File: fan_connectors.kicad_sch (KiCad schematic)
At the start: 4 parts, among them J1701 Molex 470531000, J1702 HC-1.0-4PLT

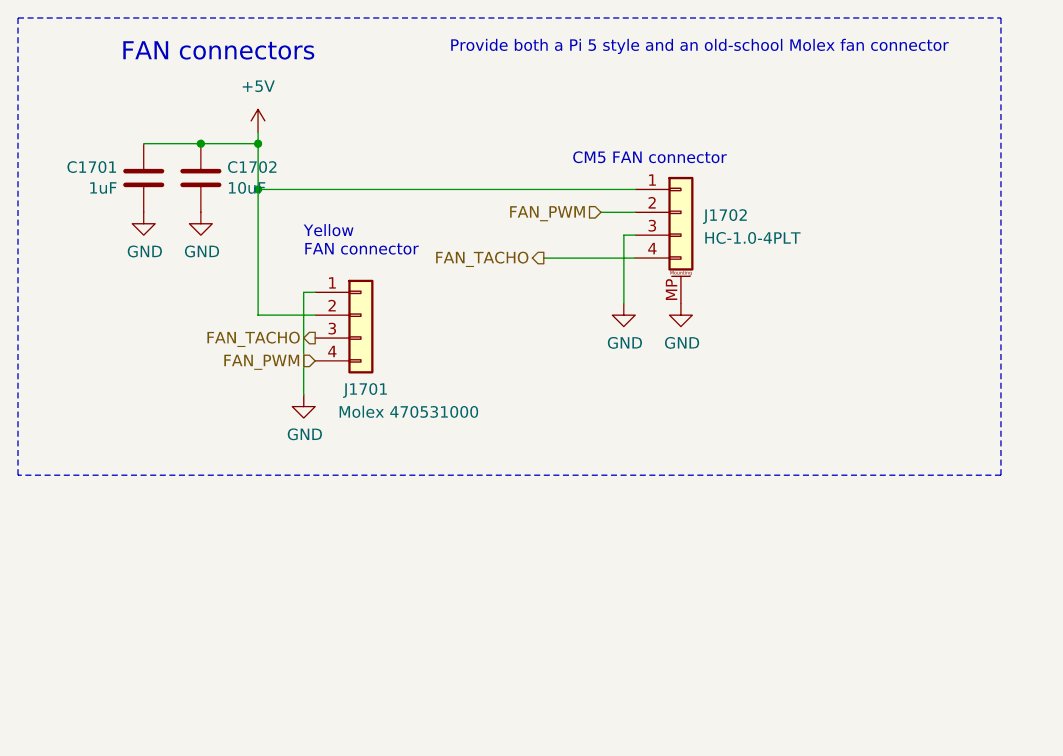
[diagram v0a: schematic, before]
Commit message: Remove Molex fan connector, add another CM5 connector to board bottom
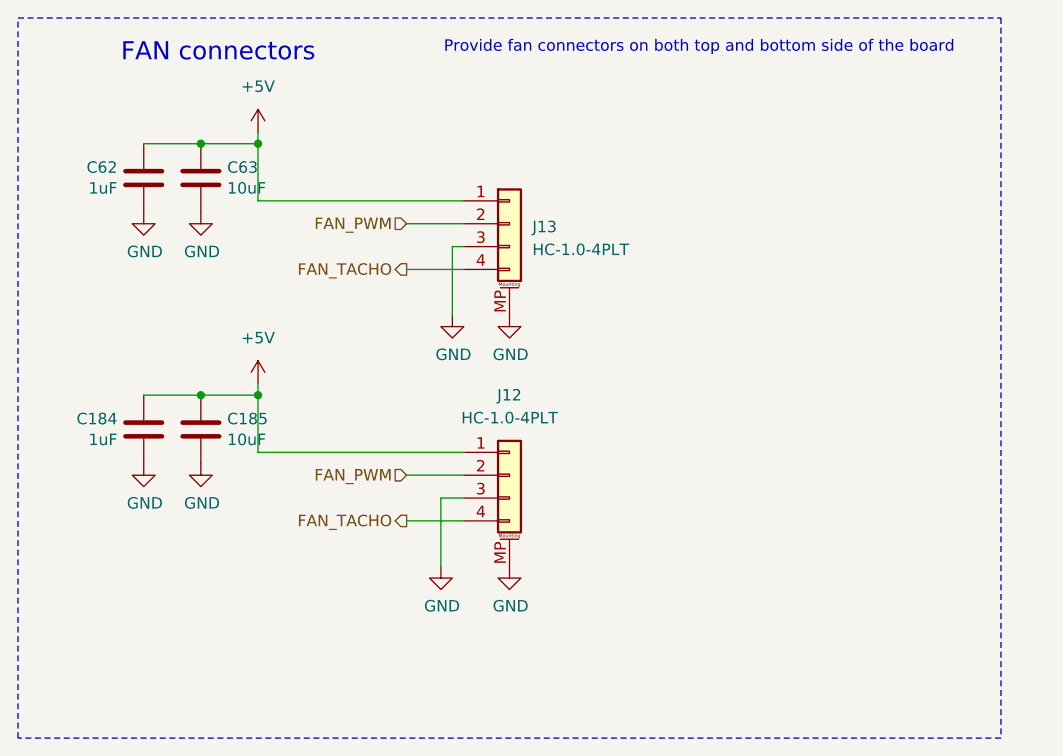
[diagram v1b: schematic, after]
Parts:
- removed J1701: Molex 470531000, Connector:FanPinHeader_1x04_P2.54mm_Vertical, symbol Connector_Generic:Conn_01x04
- added C184: 1uF, Capacitor_SMD:C_0402_1005Metric, symbol Device:C
- added C185: 10uF, Capacitor_SMD:C_0603_1608Metric, symbol Device:C
- added J12: HC-1.0-4PLT, Hatlabs:JST_SH_HCTL_HC-1.0-4PLT_1x04-1MP_P1.00mm_Vertical, symbol Connector_Generic_MountingPin:Conn_01x04_MountingPin
- renumbered C1701 to C62, C1702 to C63, J1702 to J13
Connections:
- net +5V: now also C184.1, C185.1, J12.1 (Pin_1)
- net FAN_PWM: now also J12.2 (Pin_2)
- net FAN_TACHO: now also J12.4 (Pin_4)
- net GND: now also C184.2, C185.2, J12.3 (Pin_3), J12.MP (MountPin)
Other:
- note added: "Provide fan connectors on both top and bottom side of the board"
- note removed: "CM5 FAN connector"
- note removed: "Provide both a Pi 5 style and an old-school Molex fan connector"
- note removed: "Yellow FAN connector"
- moved on the sheet: J13

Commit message: Reannotate the board
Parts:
- renumbered C62 to C61, C184 to C62, C185 to C64, J13 to J12, J12 to J13
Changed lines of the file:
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@@
 		(on_board yes)
 		(dnp no)
-		(property "Reference" "#PWR0106"
+		(property "Reference" "#PWR0104"
 			(at 133.35 107.95 0)
 			(effects
@@
 			(project "HALPI2"
 				(path "/abc482bd-3f17-4d35-80db-1da3dcdb5c27/7c248bd3-8232-4777-a40c-eab53460cf85/1b14d1cb-dda2-44c5-97d1-a618f21bed66"
-					(reference "#PWR0106")
+					(reference "#PWR0104")
 					(unit 1)
 				)
@@
 		(on_board yes)
 		(dnp no)
-		(property "Reference" "C62"
+		(property "Reference" "C61"
 			(at 96.139 85.1916 0)
 			(effects
@@
 			(project "HALPI2"
 				(path "/abc482bd-3f17-4d35-80db-1da3dcdb5c27/7c248bd3-8232-4777-a40c-eab53460cf85/1b14d1cb-dda2-44c5-97d1-a618f21bed66"
-					(reference "C62")
+					(reference "C61")
 					(unit 1)
 				)
@@
 		(on_board yes)
 		(dnp no)
-		(property "Reference" "#PWR0102"
+		(property "Reference" "#PWR099"
 			(at 105.41 96.52 0)
 			(effects
@@
 			(project "HALPI2"
 				(path "/abc482bd-3f17-4d35-80db-1da3dcdb5c27/7c248bd3-8232-4777-a40c-eab53460cf85/1b14d1cb-dda2-44c5-97d1-a618f21bed66"
-					(reference "#PWR0102")
+					(reference "#PWR099")
 					(unit 1)
 				)
@@
 		(on_board yes)
 		(dnp no)
-		(property "Reference" "#PWR0101"
+		(property "Reference" "#PWR097"
 			(at 99.06 96.52 0)
 			(effects
@@
 			(project "HALPI2"
 				(path "/abc482bd-3f17-4d35-80db-1da3dcdb5c27/7c248bd3-8232-4777-a40c-eab53460cf85/1b14d1cb-dda2-44c5-97d1-a618f21bed66"
-					(reference "#PWR0101")
+					(reference "#PWR097")
 					(unit 1)
 				)
@@
 		(on_board yes)
 		(dnp no)
-		(property "Reference" "#PWR0355"
+		(property "Reference" "#PWR0100"
 			(at 105.41 124.46 0)
 			(effects
@@
 			(project "HALPI2"
 				(path "/abc482bd-3f17-4d35-80db-1da3dcdb5c27/7c248bd3-8232-4777-a40c-eab53460cf85/1b14d1cb-dda2-44c5-97d1-a618f21bed66"
-					(reference "#PWR0355")
+					(reference "#PWR0100")
 					(unit 1)
 				)
@@
 		(on_board yes)
 		(dnp no)
-		(property "Reference" "C185"
+		(property "Reference" "C64"
 			(at 108.331 113.1316 0)
 			(effects
@@
 			(project "HALPI2"
 				(path "/abc482bd-3f17-4d35-80db-1da3dcdb5c27/7c248bd3-8232-4777-a40c-eab53460cf85/1b14d1cb-dda2-44c5-97d1-a618f21bed66"
-					(reference "C185")
+					(reference "C64")
 					(unit 1)
 				)
@@
 		(on_board yes)
 		(dnp no)
-		(property "Reference" "#PWR0104"
+		(property "Reference" "#PWR0103"
 			(at 132.08 135.89 0)
 			(effects
@@
 			(project "HALPI2"
 				(path "/abc482bd-3f17-4d35-80db-1da3dcdb5c27/7c248bd3-8232-4777-a40c-eab53460cf85/1b14d1cb-dda2-44c5-97d1-a618f21bed66"
-					(reference "#PWR0104")
+					(reference "#PWR0103")
 					(unit 1)
 				)
@@
 		(on_board yes)
 		(dnp no)
-		(property "Reference" "#PWR0354"
+		(property "Reference" "#PWR098"
 			(at 99.06 124.46 0)
 			(effects
@@
 			(project "HALPI2"
 				(path "/abc482bd-3f17-4d35-80db-1da3dcdb5c27/7c248bd3-8232-4777-a40c-eab53460cf85/1b14d1cb-dda2-44c5-97d1-a618f21bed66"
-					(reference "#PWR0354")
+					(reference "#PWR098")
 					(unit 1)
 				)
@@
 		(dnp no)
 		(fields_autoplaced yes)
-		(property "Reference" "#PWR0103"
+		(property "Reference" "#PWR0101"
 			(at 111.76 85.09 0)
 			(effects
@@
 			(project "HALPI2"
 				(path "/abc482bd-3f17-4d35-80db-1da3dcdb5c27/7c248bd3-8232-4777-a40c-eab53460cf85/1b14d1cb-dda2-44c5-97d1-a618f21bed66"
-					(reference "#PWR0103")
+					(reference "#PWR0101")
 					(unit 1)
 				)
@@
 		(dnp no)
 		(fields_autoplaced yes)
-		(property "Reference" "#PWR0356"
+		(property "Reference" "#PWR0102"
 			(at 111.76 113.03 0)
 			(effects
@@
 			(project "HALPI2"
 				(path "/abc482bd-3f17-4d35-80db-1da3dcdb5c27/7c248bd3-8232-4777-a40c-eab53460cf85/1b14d1cb-dda2-44c5-97d1-a618f21bed66"
-					(reference "#PWR0356")
+					(reference "#PWR0102")
 					(unit 1)
 				)
@@
 		(on_board yes)
 		(dnp no)
-		(property "Reference" "#PWR0107"
+		(property "Reference" "#PWR0105"
 			(at 139.7 107.95 0)
 			(effects
@@
 			(project "HALPI2"
 				(path "/abc482bd-3f17-4d35-80db-1da3dcdb5c27/7c248bd3-8232-4777-a40c-eab53460cf85/1b14d1cb-dda2-44c5-97d1-a618f21bed66"
-					(reference "#PWR0107")
+					(reference "#PWR0105")
 					(unit 1)
 				)
@@
 		(on_board yes)
 		(dnp no)
-		(property "Reference" "C184"
+		(property "Reference" "C62"
 			(at 96.139 113.1316 0)
 			(effects
@@
 			(project "HALPI2"
 				(path "/abc482bd-3f17-4d35-80db-1da3dcdb5c27/7c248bd3-8232-4777-a40c-eab53460cf85/1b14d1cb-dda2-44c5-97d1-a618f21bed66"
-					(reference "C184")
+					(reference "C62")
 					(unit 1)
 				)
@@
 		(dnp no)
 		(fields_autoplaced yes)
-		(property "Reference" "J13"
+		(property "Reference" "J12"
 			(at 142.24 91.7955 0)
 			(effects
@@
 			(project "HALPI2"
 				(path "/abc482bd-3f17-4d35-80db-1da3dcdb5c27/7c248bd3-8232-4777-a40c-eab53460cf85/1b14d1cb-dda2-44c5-97d1-a618f21bed66"
-					(reference "J13")
+					(reference "J12")
 					(unit 1)
 				)
@@
 		(dnp no)
 		(fields_autoplaced yes)
-		(property "Reference" "J12"
+		(property "Reference" "J13"
 			(at 139.7 110.49 0)
 			(effects
@@
 			(project "HALPI2"
 				(path "/abc482bd-3f17-4d35-80db-1da3dcdb5c27/7c248bd3-8232-4777-a40c-eab53460cf85/1b14d1cb-dda2-44c5-97d1-a618f21bed66"
-					(reference "J12")
+					(reference "J13")
 					(unit 1)
 				)
@@
 		(on_board yes)
 		(dnp no)
-		(property "Reference" "#PWR0105"
+		(property "Reference" "#PWR0106"
 			(at 139.7 135.89 0)
 			(effects
@@
 			(project "HALPI2"
 				(path "/abc482bd-3f17-4d35-80db-1da3dcdb5c27/7c248bd3-8232-4777-a40c-eab53460cf85/1b14d1cb-dda2-44c5-97d1-a618f21bed66"
-					(reference "#PWR0105")
-					(unit 1)
-				)
+					(reference "#PWR0106")
+					(unit 1)
+				)

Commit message: FInal v0.2.0 proto changes
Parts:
- renumbered C61 to C63, C62 to C64, C63 to C65, C64 to C66
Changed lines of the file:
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@@
 		(on_board yes)
 		(dnp no)
-		(property "Reference" "C63"
+		(property "Reference" "C65"
 			(at 108.331 85.1916 0)
 			(effects
@@
 			(project "HALPI2"
 				(path "/abc482bd-3f17-4d35-80db-1da3dcdb5c27/7c248bd3-8232-4777-a40c-eab53460cf85/1b14d1cb-dda2-44c5-97d1-a618f21bed66"
-					(reference "C63")
+					(reference "C65")
 					(unit 1)
 				)
@@
 		(on_board yes)
 		(dnp no)
-		(property "Reference" "#PWR0104"
+		(property "Reference" "#PWR0105"
 			(at 133.35 107.95 0)
 			(effects
@@
 			(project "HALPI2"
 				(path "/abc482bd-3f17-4d35-80db-1da3dcdb5c27/7c248bd3-8232-4777-a40c-eab53460cf85/1b14d1cb-dda2-44c5-97d1-a618f21bed66"
-					(reference "#PWR0104")
+					(reference "#PWR0105")
 					(unit 1)
 				)
@@
 		(on_board yes)
 		(dnp no)
-		(property "Reference" "C61"
+		(property "Reference" "C63"
 			(at 96.139 85.1916 0)
 			(effects
@@
 			(project "HALPI2"
 				(path "/abc482bd-3f17-4d35-80db-1da3dcdb5c27/7c248bd3-8232-4777-a40c-eab53460cf85/1b14d1cb-dda2-44c5-97d1-a618f21bed66"
-					(reference "C61")
+					(reference "C63")
 					(unit 1)
 				)
@@
 		(on_board yes)
 		(dnp no)
-		(property "Reference" "#PWR099"
+		(property "Reference" "#PWR0100"
 			(at 105.41 96.52 0)
 			(effects
@@
 			(project "HALPI2"
 				(path "/abc482bd-3f17-4d35-80db-1da3dcdb5c27/7c248bd3-8232-4777-a40c-eab53460cf85/1b14d1cb-dda2-44c5-97d1-a618f21bed66"
-					(reference "#PWR099")
+					(reference "#PWR0100")
 					(unit 1)
 				)
@@
 		(on_board yes)
 		(dnp no)
-		(property "Reference" "#PWR097"
+		(property "Reference" "#PWR098"
 			(at 99.06 96.52 0)
 			(effects
@@
 			(project "HALPI2"
 				(path "/abc482bd-3f17-4d35-80db-1da3dcdb5c27/7c248bd3-8232-4777-a40c-eab53460cf85/1b14d1cb-dda2-44c5-97d1-a618f21bed66"
-					(reference "#PWR097")
+					(reference "#PWR098")
 					(unit 1)
 				)
@@
 		(on_board yes)
 		(dnp no)
-		(property "Reference" "#PWR0100"
+		(property "Reference" "#PWR0101"
 			(at 105.41 124.46 0)
 			(effects
@@
 			(project "HALPI2"
 				(path "/abc482bd-3f17-4d35-80db-1da3dcdb5c27/7c248bd3-8232-4777-a40c-eab53460cf85/1b14d1cb-dda2-44c5-97d1-a618f21bed66"
-					(reference "#PWR0100")
+					(reference "#PWR0101")
 					(unit 1)
 				)
@@
 		(on_board yes)
 		(dnp no)
-		(property "Reference" "C64"
+		(property "Reference" "C66"
 			(at 108.331 113.1316 0)
 			(effects
@@
 			(project "HALPI2"
 				(path "/abc482bd-3f17-4d35-80db-1da3dcdb5c27/7c248bd3-8232-4777-a40c-eab53460cf85/1b14d1cb-dda2-44c5-97d1-a618f21bed66"
-					(reference "C64")
+					(reference "C66")
 					(unit 1)
 				)
@@
 		(on_board yes)
 		(dnp no)
-		(property "Reference" "#PWR0103"
+		(property "Reference" "#PWR0104"
 			(at 132.08 135.89 0)
 			(effects
@@
 			(project "HALPI2"
 				(path "/abc482bd-3f17-4d35-80db-1da3dcdb5c27/7c248bd3-8232-4777-a40c-eab53460cf85/1b14d1cb-dda2-44c5-97d1-a618f21bed66"
-					(reference "#PWR0103")
+					(reference "#PWR0104")
 					(unit 1)
 				)
@@
 		(on_board yes)
 		(dnp no)
-		(property "Reference" "#PWR098"
+		(property "Reference" "#PWR099"
 			(at 99.06 124.46 0)
 			(effects
@@
 			(project "HALPI2"
 				(path "/abc482bd-3f17-4d35-80db-1da3dcdb5c27/7c248bd3-8232-4777-a40c-eab53460cf85/1b14d1cb-dda2-44c5-97d1-a618f21bed66"
-					(reference "#PWR098")
+					(reference "#PWR099")
 					(unit 1)
 				)
@@
 		(dnp no)
 		(fields_autoplaced yes)
-		(property "Reference" "#PWR0101"
+		(property "Reference" "#PWR0102"
 			(at 111.76 85.09 0)
 			(effects
@@
 			(project "HALPI2"
 				(path "/abc482bd-3f17-4d35-80db-1da3dcdb5c27/7c248bd3-8232-4777-a40c-eab53460cf85/1b14d1cb-dda2-44c5-97d1-a618f21bed66"
-					(reference "#PWR0101")
+					(reference "#PWR0102")
 					(unit 1)
 				)
@@
 		(dnp no)
 		(fields_autoplaced yes)
-		(property "Reference" "#PWR0102"
+		(property "Reference" "#PWR0103"
 			(at 111.76 113.03 0)
 			(effects
@@
 			(project "HALPI2"
 				(path "/abc482bd-3f17-4d35-80db-1da3dcdb5c27/7c248bd3-8232-4777-a40c-eab53460cf85/1b14d1cb-dda2-44c5-97d1-a618f21bed66"
-					(reference "#PWR0102")
+					(reference "#PWR0103")
 					(unit 1)
 				)
@@
 		(on_board yes)
 		(dnp no)
-		(property "Reference" "#PWR0105"
+		(property "Reference" "#PWR0106"
 			(at 139.7 107.95 0)
 			(effects
@@
 			(project "HALPI2"
 				(path "/abc482bd-3f17-4d35-80db-1da3dcdb5c27/7c248bd3-8232-4777-a40c-eab53460cf85/1b14d1cb-dda2-44c5-97d1-a618f21bed66"
-					(reference "#PWR0105")
+					(reference "#PWR0106")
 					(unit 1)
 				)
@@
 		(on_board yes)
 		(dnp no)
-		(property "Reference" "C62"
+		(property "Reference" "C64"
 			(at 96.139 113.1316 0)
 			(effects
@@
 			(project "HALPI2"
 				(path "/abc482bd-3f17-4d35-80db-1da3dcdb5c27/7c248bd3-8232-4777-a40c-eab53460cf85/1b14d1cb-dda2-44c5-97d1-a618f21bed66"
-					(reference "C62")
+					(reference "C64")
 					(unit 1)
 				)
@@
 		(on_board yes)
 		(dnp no)
-		(property "Reference" "#PWR0106"
+		(property "Reference" "#PWR0107"
 			(at 139.7 135.89 0)
 			(effects
@@
 			(project "HALPI2"
 				(path "/abc482bd-3f17-4d35-80db-1da3dcdb5c27/7c248bd3-8232-4777-a40c-eab53460cf85/1b14d1cb-dda2-44c5-97d1-a618f21bed66"
-					(reference "#PWR0106")
-					(unit 1)
-				)
+					(reference "#PWR0107")
+					(unit 1)
+				)

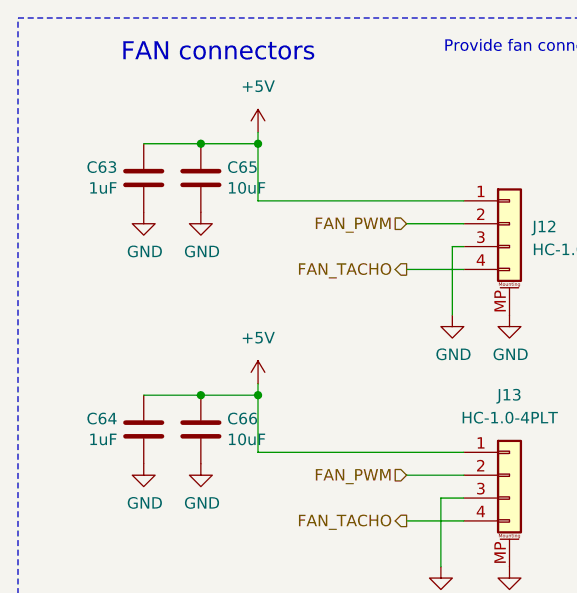
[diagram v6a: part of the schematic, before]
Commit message: Final chores
- Reannotate components
- Improve USB2 connector skew matching
- Update sheet blocks
- Fix some diff-pair double-inversions
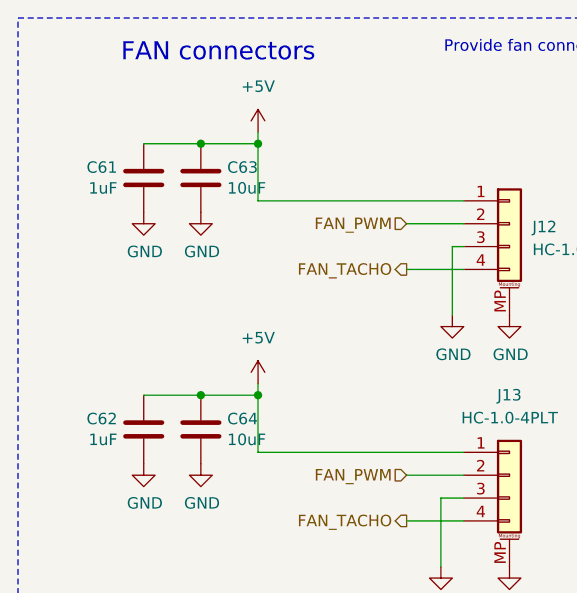
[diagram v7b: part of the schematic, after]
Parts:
- renumbered C63 to C61, C64 to C62, C65 to C63, C66 to C64
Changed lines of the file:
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@@
 	(title_block
 		(title "HALPI2")
-		(date "2025-03-27")
-		(rev "v0.2.0")
+		(date "2025-05-08")
+		(rev "v0.3.0")
 		(company "Hat Labs Oy")
 		(comment 1 "https://ohwr.org/cern_ohl_s_v2.pdf")
@@
 		(on_board yes)
 		(dnp no)
-		(property "Reference" "C65"
+		(property "Reference" "C63"
 			(at 108.331 85.1916 0)
 			(effects
@@
 			(project "HALPI2"
 				(path "/abc482bd-3f17-4d35-80db-1da3dcdb5c27/7c248bd3-8232-4777-a40c-eab53460cf85/1b14d1cb-dda2-44c5-97d1-a618f21bed66"
-					(reference "C65")
+					(reference "C63")
 					(unit 1)
 				)
@@
 		(on_board yes)
 		(dnp no)
-		(property "Reference" "#PWR0105"
+		(property "Reference" "#PWR099"
 			(at 133.35 107.95 0)
 			(effects
@@
 			(project "HALPI2"
 				(path "/abc482bd-3f17-4d35-80db-1da3dcdb5c27/7c248bd3-8232-4777-a40c-eab53460cf85/1b14d1cb-dda2-44c5-97d1-a618f21bed66"
-					(reference "#PWR0105")
+					(reference "#PWR099")
 					(unit 1)
 				)
@@
 		(on_board yes)
 		(dnp no)
-		(property "Reference" "C63"
+		(property "Reference" "C61"
 			(at 96.139 85.1916 0)
 			(effects
@@
 			(project "HALPI2"
 				(path "/abc482bd-3f17-4d35-80db-1da3dcdb5c27/7c248bd3-8232-4777-a40c-eab53460cf85/1b14d1cb-dda2-44c5-97d1-a618f21bed66"
-					(reference "C63")
+					(reference "C61")
 					(unit 1)
 				)
@@
 		(on_board yes)
 		(dnp no)
-		(property "Reference" "#PWR0100"
+		(property "Reference" "#PWR094"
 			(at 105.41 96.52 0)
 			(effects
@@
 			(project "HALPI2"
 				(path "/abc482bd-3f17-4d35-80db-1da3dcdb5c27/7c248bd3-8232-4777-a40c-eab53460cf85/1b14d1cb-dda2-44c5-97d1-a618f21bed66"
-					(reference "#PWR0100")
+					(reference "#PWR094")
 					(unit 1)
 				)
@@
 		(on_board yes)
 		(dnp no)
-		(property "Reference" "#PWR098"
+		(property "Reference" "#PWR092"
 			(at 99.06 96.52 0)
 			(effects
@@
 			(project "HALPI2"
 				(path "/abc482bd-3f17-4d35-80db-1da3dcdb5c27/7c248bd3-8232-4777-a40c-eab53460cf85/1b14d1cb-dda2-44c5-97d1-a618f21bed66"
-					(reference "#PWR098")
+					(reference "#PWR092")
 					(unit 1)
 				)
@@
 		(on_board yes)
 		(dnp no)
-		(property "Reference" "#PWR0101"
+		(property "Reference" "#PWR095"
 			(at 105.41 124.46 0)
 			(effects
@@
 			(project "HALPI2"
 				(path "/abc482bd-3f17-4d35-80db-1da3dcdb5c27/7c248bd3-8232-4777-a40c-eab53460cf85/1b14d1cb-dda2-44c5-97d1-a618f21bed66"
-					(reference "#PWR0101")
+					(reference "#PWR095")
 					(unit 1)
 				)
@@
 		(on_board yes)
 		(dnp no)
-		(property "Reference" "C66"
+		(property "Reference" "C64"
 			(at 108.331 113.1316 0)
 			(effects
@@
 			(project "HALPI2"
 				(path "/abc482bd-3f17-4d35-80db-1da3dcdb5c27/7c248bd3-8232-4777-a40c-eab53460cf85/1b14d1cb-dda2-44c5-97d1-a618f21bed66"
-					(reference "C66")
+					(reference "C64")
 					(unit 1)
 				)
@@
 		(on_board yes)
 		(dnp no)
-		(property "Reference" "#PWR0104"
+		(property "Reference" "#PWR098"
 			(at 132.08 135.89 0)
 			(effects
@@
 			(project "HALPI2"
 				(path "/abc482bd-3f17-4d35-80db-1da3dcdb5c27/7c248bd3-8232-4777-a40c-eab53460cf85/1b14d1cb-dda2-44c5-97d1-a618f21bed66"
-					(reference "#PWR0104")
+					(reference "#PWR098")
 					(unit 1)
 				)
@@
 		(on_board yes)
 		(dnp no)
-		(property "Reference" "#PWR099"
+		(property "Reference" "#PWR093"
 			(at 99.06 124.46 0)
 			(effects
@@
 			(project "HALPI2"
 				(path "/abc482bd-3f17-4d35-80db-1da3dcdb5c27/7c248bd3-8232-4777-a40c-eab53460cf85/1b14d1cb-dda2-44c5-97d1-a618f21bed66"
-					(reference "#PWR099")
+					(reference "#PWR093")
 					(unit 1)
 				)
@@
 		(dnp no)
 		(fields_autoplaced yes)
-		(property "Reference" "#PWR0102"
+		(property "Reference" "#PWR096"
 			(at 111.76 85.09 0)
 			(effects
@@
 			(project "HALPI2"
 				(path "/abc482bd-3f17-4d35-80db-1da3dcdb5c27/7c248bd3-8232-4777-a40c-eab53460cf85/1b14d1cb-dda2-44c5-97d1-a618f21bed66"
-					(reference "#PWR0102")
+					(reference "#PWR096")
 					(unit 1)
 				)
@@
 		(dnp no)
 		(fields_autoplaced yes)
-		(property "Reference" "#PWR0103"
+		(property "Reference" "#PWR097"
 			(at 111.76 113.03 0)
 			(effects
@@
 			(project "HALPI2"
 				(path "/abc482bd-3f17-4d35-80db-1da3dcdb5c27/7c248bd3-8232-4777-a40c-eab53460cf85/1b14d1cb-dda2-44c5-97d1-a618f21bed66"
-					(reference "#PWR0103")
+					(reference "#PWR097")
 					(unit 1)
 				)
@@
 		(on_board yes)
 		(dnp no)
-		(property "Reference" "#PWR0106"
+		(property "Reference" "#PWR0100"
 			(at 139.7 107.95 0)
 			(effects
@@
 			(project "HALPI2"
 				(path "/abc482bd-3f17-4d35-80db-1da3dcdb5c27/7c248bd3-8232-4777-a40c-eab53460cf85/1b14d1cb-dda2-44c5-97d1-a618f21bed66"
-					(reference "#PWR0106")
+					(reference "#PWR0100")
 					(unit 1)
 				)
@@
 		(on_board yes)
 		(dnp no)
-		(property "Reference" "C64"
+		(property "Reference" "C62"
 			(at 96.139 113.1316 0)
 			(effects
@@
 			(project "HALPI2"
 				(path "/abc482bd-3f17-4d35-80db-1da3dcdb5c27/7c248bd3-8232-4777-a40c-eab53460cf85/1b14d1cb-dda2-44c5-97d1-a618f21bed66"
-					(reference "C64")
+					(reference "C62")
 					(unit 1)
 				)
@@
 		(on_board yes)
 		(dnp no)
-		(property "Reference" "#PWR0107"
+		(property "Reference" "#PWR0101"
 			(at 139.7 135.89 0)
 			(effects
@@
 			(project "HALPI2"
 				(path "/abc482bd-3f17-4d35-80db-1da3dcdb5c27/7c248bd3-8232-4777-a40c-eab53460cf85/1b14d1cb-dda2-44c5-97d1-a618f21bed66"
-					(reference "#PWR0107")
-					(unit 1)
-				)
+					(reference "#PWR0101")
+					(unit 1)
+				)
